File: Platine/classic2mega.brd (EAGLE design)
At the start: 57.5 x 44.5 mm, 31 parts, among them IC1 MEGA16-A, IC2 74HC157D, Q2 16MHz, X2 NEB21R

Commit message: New board revison
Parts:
- removed JP1: Megadrive Power, jumper:JP1
- removed R9: EZJZ1V120KA, varistor:CT/CN0603
- removed U$4: TSM2310, TSM2310:SOT23
- removed X2: NEB21R, con-lumberg:NEB21R
- moved R5 10.9 mm to (47.4, 49.1), flipped to the top
- moved Q2 7.00 mm to (42.2, 23.3)
- moved C2 6.71 mm to (40.9, 28.2), flipped to the top, turned to 90 degrees
- moved C3 5.69 mm to (43.7, 28.3), flipped to the top, turned to 90 degrees
- moved R8 5.29 mm to (64.9, 28.8)
- moved R3 4.94 mm to (30.8, 51.9), flipped to the top, turned to 0 degrees
- moved R2 4.07 mm to (30.8, 48.0), flipped to the top, turned to 0 degrees
- moved R6 2.53 mm to (41.9, 38.5), turned to 0 degrees
- moved IC1 2.34 mm to (42.0, 38.3)
- moved C1 2.12 mm to (41.3, 48.8), turned to 270 degrees
- renumbered U$1 to U1, U$2 to U2, U$3 to H1
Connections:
- removed net CON_CD32_SELECT: JP1.1, X1.5
- removed net N$10: R9.2, U$4.3, X2.3
- net 5V: now also X1.5; no longer JP1.2, R9.1, U$4.1, X2.1
- net GND: no longer U$4.2
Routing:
- net GND: track 301.1 -> 335.4 mm, vias 4 -> 2
- net N$4: track 53.9 -> 21.0 mm
- net PAD_DOWN: track 37.0 -> 56.8 mm, vias 0 -> 1
- net PAD_UP: track 52.3 -> 34.0 mm, vias 1 -> 2
- net N$10: track 17.8 -> 0.00 mm
- net PAD_B: track 28.4 -> 41.7 mm
- net SDA: track 42.6 -> 31.3 mm
- net PAD_RIGHT: track 92.6 -> 81.7 mm, vias 2 -> 0
- net CON_AB: track 29.2 -> 19.1 mm, vias 1 -> 0
- net PAD_C: track 31.5 -> 22.5 mm
- net N$1: track 23.9 -> 15.6 mm, vias 3 -> 0
- net CON_CD32_SELECT: track 6.49 -> 0.00 mm
- net N$2: track 17.4 -> 11.6 mm
- net 5V: track 177.8 -> 172.6 mm, vias 4 -> 3
- net RESET: track 37.1 -> 32.0 mm
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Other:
- board text added: "1"
- board text added: "16"
- board text added: "8"
- board text added: "Classic2Mega 1.1"

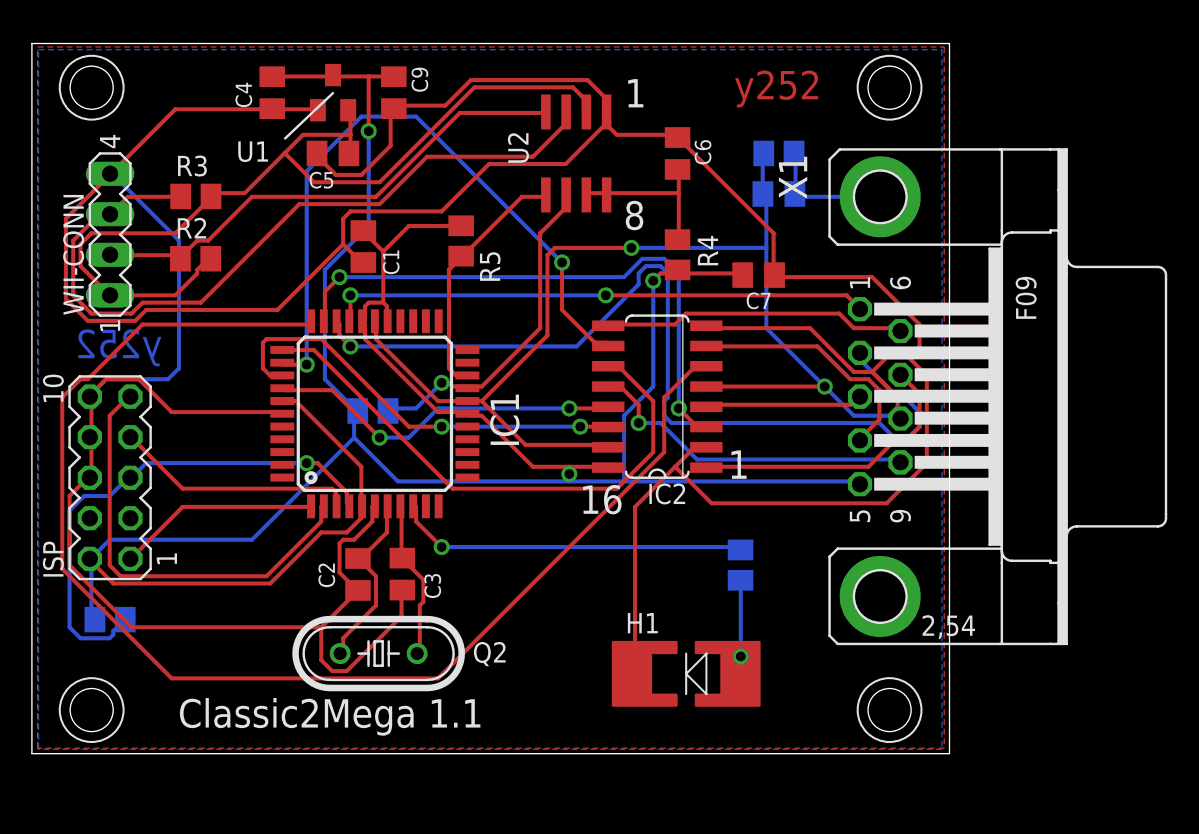
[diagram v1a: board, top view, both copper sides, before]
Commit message: Replace i2c level shifter with discrete components
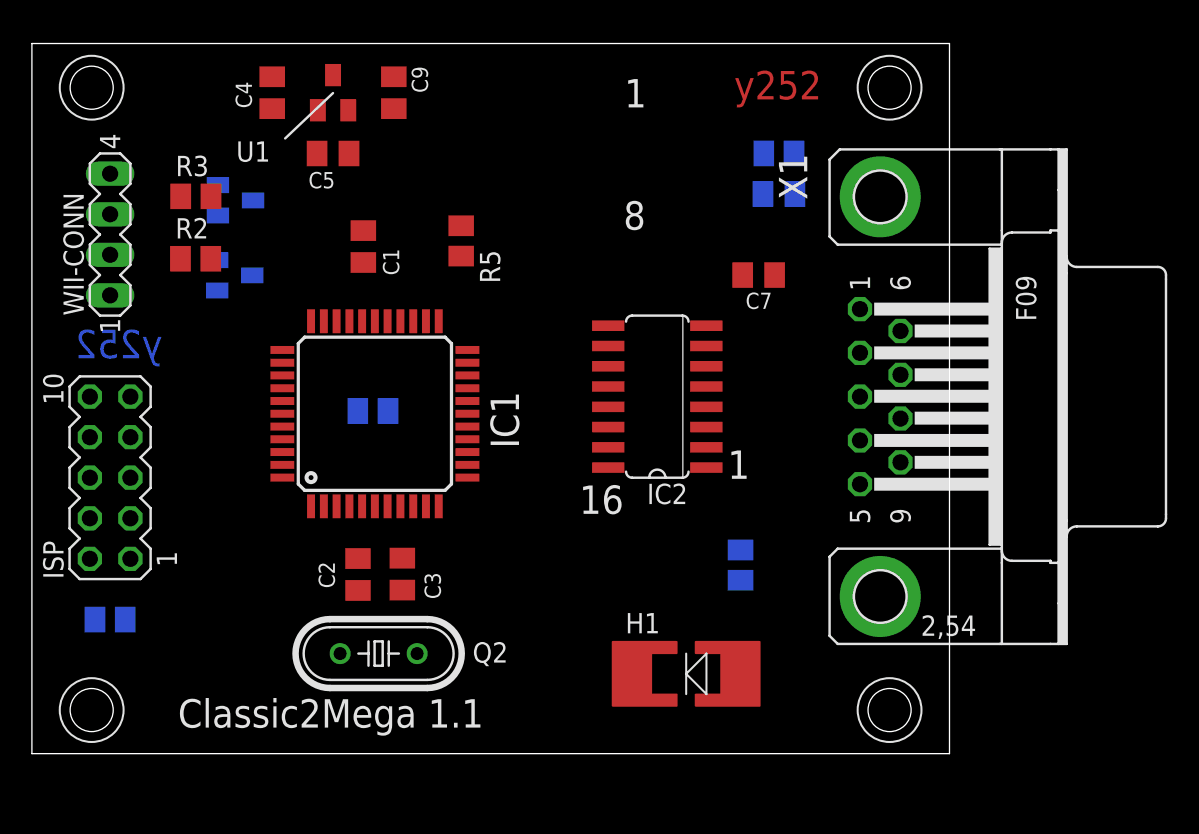
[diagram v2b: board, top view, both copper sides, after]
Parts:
- removed C6: 100n, resistor:C0805K
- removed R4: 200k, resistor:M0805
- removed U2: PCA9306_SO8, PCA9306:SO08
- added U$1, U$2: BSS138_SOT23, BSS138:SOT23
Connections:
- removed net N$5: C6.2, R4.1, U2.7, U2.8
- net 3.3V: now also U$1.1, U$2.1; no longer U2.2
- net 5V: no longer R4.2
- net GND: no longer C6.1, U2.1
- net N$1: now also U$2.3; no longer U2.5
- net N$4: now also U$1.3; no longer U2.6
- net SCL: now also U$1.2; no longer U2.3
- net SDA: now also U$2.2; no longer U2.4
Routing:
- net GND: track 335.4 -> 0.00 mm, vias 2 -> 0
- net 5V: track 172.6 -> 0.00 mm, vias 3 -> 0
- net PAD_RIGHT: track 81.7 -> 0.00 mm
- net 3.3V: track 57.3 -> 0.00 mm
- net PAD_DOWN: track 56.8 -> 0.00 mm, vias 1 -> 0
- net SCL: track 48.3 -> 0.00 mm
- net PAD_B: track 41.7 -> 0.00 mm, vias 2 -> 0
- net PAD_LEFT: track 36.0 -> 0.00 mm, vias 2 -> 0
- net PAD_A: track 34.7 -> 0.00 mm
- net PAD_UP: track 34.0 -> 0.00 mm, vias 2 -> 0
- net RESET: track 32.0 -> 0.00 mm, vias 1 -> 0
- net SDA: track 31.3 -> 0.00 mm
- net MISO: track 27.2 -> 0.00 mm
- net PAD_START: track 27.0 -> 0.00 mm, vias 2 -> 0
- net PAD_C: track 22.5 -> 0.00 mm, vias 2 -> 0
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- removed copper zone on layer 1, net GND
- removed copper zone on layer 16, net GND

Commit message: Change ICs to DIP packages
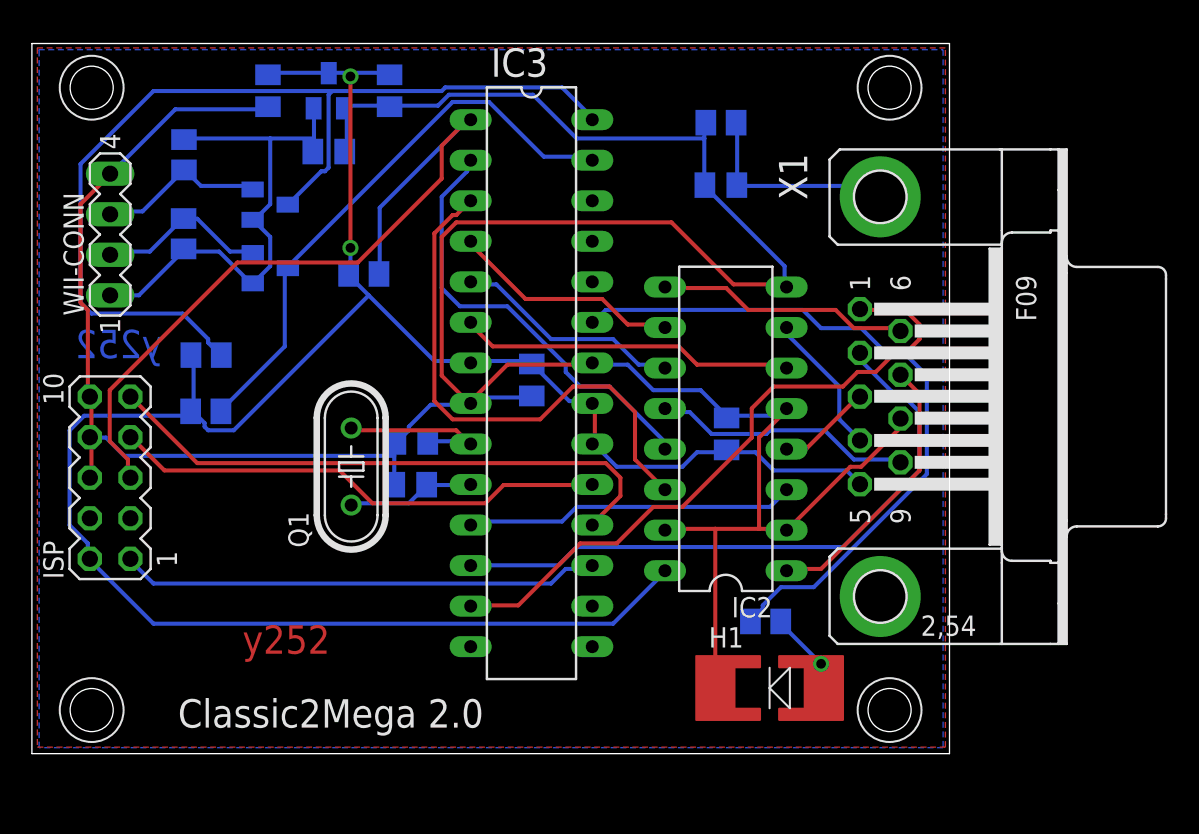
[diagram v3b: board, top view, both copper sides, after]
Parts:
- removed C1: 100n, resistor:C0805K
- removed IC1: MEGA16-A, atmega16:TQFP44
- removed Q2: 16MHz, crystal:HC49/S
- removed R1: 10k, resistor:M0805
- removed U$1, U$2: BSS138_SOT23, BSS138:SOT23
- added C6: 22p, resistor:C0805K
- added IC3: MEGA8-P, atmel:DIL28-3
- added Q1: (no value), crystal:HC49/S
- added R4: 10k, resistor:M0805
- added U2, U3: BSS138_SOT23, BSS138:SOT23
- C2: value 22p -> 100n
- IC2: value 74HC157D -> 74HC157N; device 74xx-eu:SO16 -> 74xx-eu:DIL16
- moved R5 19.2 mm to (31.4, 38.5), flipped to the bottom, turned to 0 degrees
- moved C2 16.3 mm to (51.8, 40.4), flipped to the bottom, turned to 270 degrees
- moved R6 11.0 mm to (31.4, 42.0)
- moved C7 10.2 mm to (64.0, 37.0), flipped to the bottom, turned to 270 degrees
- moved C3 8.30 mm to (44.3, 36.5), flipped to the bottom, turned to 180 degrees
- moved C9 7.89 mm to (35.3, 58.5), flipped to the bottom
- moved C4 7.35 mm to (42.9, 58.5), flipped to the bottom
- moved H1 5.30 mm to (66.7, 21.1)
- moved IC2 4.74 mm to (64.0, 37.4)
- moved R7 4.11 mm to (63.7, 56.5)
- moved R8 3.87 mm to (66.5, 25.3), turned to 180 degrees
- moved C8 3.68 mm to (63.7, 52.6)
- moved R3 2.71 mm to (30.0, 54.5), flipped to the bottom, turned to 90 degrees
- moved R2 1.74 mm to (30.0, 49.6), flipped to the bottom, turned to 270 degrees
- moved C5 0.29 mm to (39.1, 54.7), flipped to the bottom
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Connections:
- removed net N$8: IC1.9, R8.1
- new net N$5: C6.1, IC3.10, Q1.1
- net 3.3V: now also U2.1, U3.1; no longer U$1.1, U$2.1
- net 5V: now also C2.1, IC3.20, IC3.21, IC3.7, R4.2; no longer C1.1, IC1.17, IC1.27, IC1.29, IC1.38, IC1.5, R1.2
- net GND: now also C2.2, C6.2, IC3.22, IC3.8; no longer C1.2, C2.1, IC1.18, IC1.28, IC1.39, IC1.6
- net MISO: now also IC3.18; no longer IC1.2
- net MOSI: now also IC3.17; no longer IC1.1
- net N$1: now also IC3.27, U2.3; no longer IC1.20, U$2.3
- net N$2: now also IC3.23, R8.1; no longer C2.2, IC1.7, Q2.2
- net N$3: now also IC3.9, Q1.2; no longer IC1.8, Q2.1
- net N$4: now also IC3.28, U3.3; no longer IC1.19, U$1.3
- net PAD_A: now also IC3.5; no longer IC1.34
- net PAD_B: now also IC3.4; no longer IC1.35
- net PAD_C: now also IC3.2; no longer IC1.37
- net PAD_DOWN: now also IC3.12; no longer IC1.31
- net PAD_LEFT: now also IC3.11; no longer IC1.32
- net PAD_RIGHT: now also IC3.6; no longer IC1.33
- net PAD_START: now also IC3.3; no longer IC1.36
- net PAD_UP: now also IC3.13; no longer IC1.30
- net RESET: now also IC3.1, R4.1; no longer IC1.4, R1.1
- net SCK: now also IC3.19; no longer IC1.3
- net SCL: now also U3.2; no longer U$1.2
- net SDA: now also U2.2; no longer U$2.2
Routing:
- net GND: track 0.00 -> 197.5 mm
- net 5V: track 0.00 -> 135.5 mm, vias 0 -> 2
- net N$4: track 0.00 -> 62.4 mm
- net RESET: track 0.00 -> 49.1 mm
- net N$2: track 0.00 -> 44.2 mm
- net PAD_UP: track 0.00 -> 41.2 mm
- net PAD_DOWN: track 0.00 -> 39.8 mm
- net MISO: track 0.00 -> 36.5 mm
- net N$1: track 0.00 -> 35.7 mm
- net PAD_START: track 0.00 -> 33.8 mm
- net 3.3V: track 0.00 -> 32.6 mm
- net SCK: track 0.00 -> 31.1 mm
- net MOSI: track 0.00 -> 30.2 mm
- net PAD_C: track 0.00 -> 27.6 mm
- net PAD_RIGHT: track 0.00 -> 21.1 mm
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- added copper zone on layer 1, net GND
- added copper zone on layer 16, net GND
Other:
- board text added: "Classic2Mega 2.0"
- board text removed: "1"
- board text removed: "16"
- board text removed: "8"
- board text removed: "Classic2Mega 1.1"

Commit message: Change C9 to 1210 footprint
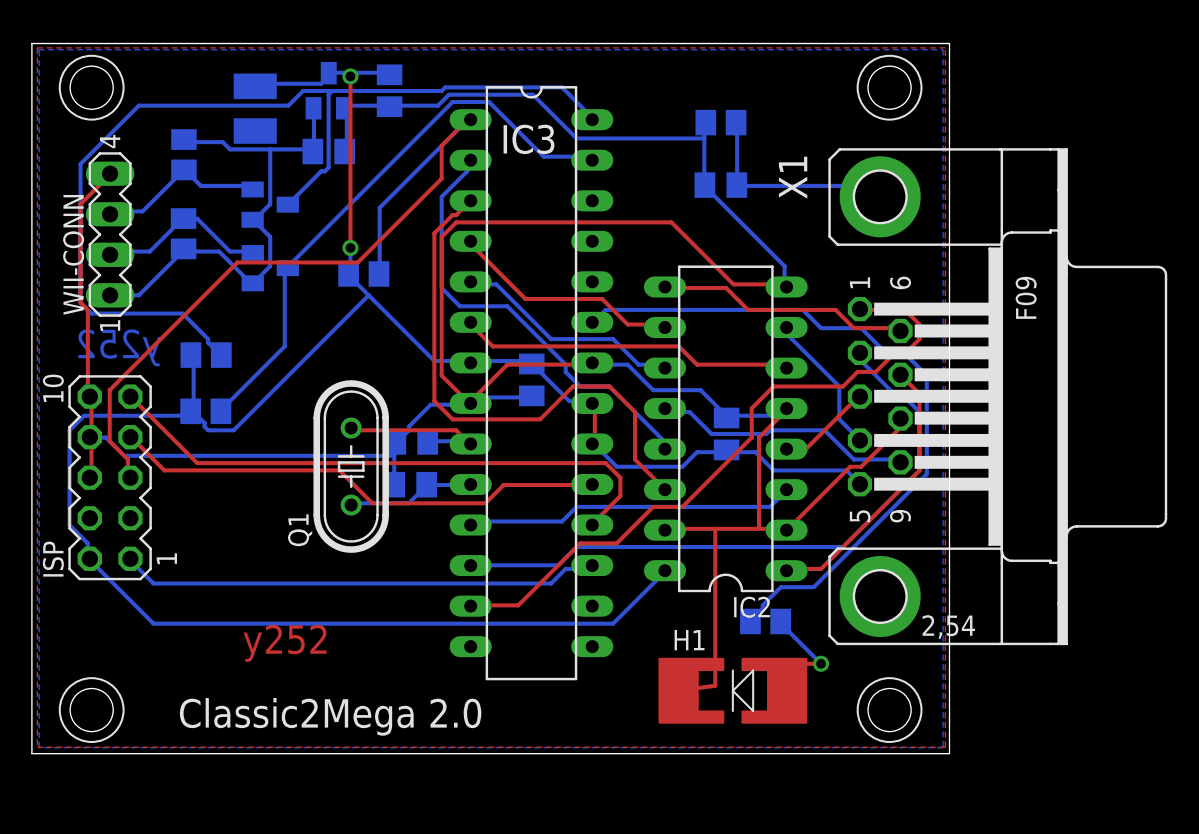
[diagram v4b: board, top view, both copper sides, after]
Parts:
- C9: device resistor:C0805K -> resistor:C1210
- moved H1 2.31 mm to (64.4, 20.9)
- moved C9 1.38 mm to (34.5, 57.4)
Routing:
- net GND: track 197.5 -> 188.2 mm
- net N$9: track 5.28 -> 7.53 mm
- net 5V: track 135.5 -> 136.8 mm
